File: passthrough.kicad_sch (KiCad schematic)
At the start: 20 parts, among them J10 MiniFit, J13 MiniFit, J5 Pixhawk 1, J6 Pixhawk 2, U17 TLA2528

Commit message: improvements with derick
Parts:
- added D20: RED, LED_SMD:LED_0603_1608Metric, symbol Device:LED
- added D22: 15V, Diode_SMD:D_SOD-523, symbol Device:D_Zener
- added Q3: MMBT5551L, Package_TO_SOT_SMD:SOT-23, symbol Transistor_BJT:MMBT5551L
- added Q4: FDC5614P, Package_TO_SOT_SMD:TSOT-23-6, symbol Transistor_FET:Q_PMOS_DGS
- added R78: 24K, Resistor_SMD:R_0402_1005Metric, symbol Device:R
- added R84: 10K, Resistor_SMD:R_0402_1005Metric, symbol Device:R
- added R85: 1K, Resistor_SMD:R_0402_1005Metric, symbol Device:R
- D15: now not fitted
- R73, R75, TP11: now left out of the parts list
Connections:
- net +BATT: now also D22.2 (A), Q4.1 (D), Q4.2 (D), Q4.5 (D), Q4.6 (D)
- net GND: now also Q3.2 (E), R78.2, R84.1
- new net: D20.1 (K), R78.1
- new net: D20.2 (A), Q4.4 (S)
- new net: D22.1 (K), Q3.3 (C), Q4.3 (G), R84.2
- new net: Q3.1 (B), R85.2
- new net ~{FAULT}: R85.1
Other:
- note added: "FAULT LED INDICATOR - 50V with 3.3V MCU Control LED ON (fault): MCU OFF or GPIO LOW LED OFF (ok): MCU ON with GPIO HIGH (3.3V) PROTECTION: Zener D1 clamps Vgs to -15V (prevents gate overvoltage) R2 pull-down ensures clean gate switchingNPN Q2 inverts logic & isolates 3.3V from 50V railR3 limits base current to safe MCU levels OPERATION: GPIO LOW → Q2 OFF → R2 pulls gate LOW → Vgs = -15V → Q1 ON →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"
- note added: "Fault LED"

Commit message: final export of r1 after changes
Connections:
- net IPAYLOAD renamed IPAYLOAD1
- net RESV0 renamed IPAYLOAD2
- net RESV1 renamed IPAYLOAD3
- net RESV2 renamed VBAT_SCALED
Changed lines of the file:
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@@
 		)
 	)
-	(hierarchical_label "RESV0"
+	(hierarchical_label "IPAYLOAD2"
 		(shape input)
 		(at 217.17 54.61 0)
@@
 		)
 	)
-	(hierarchical_label "RESV1"
+	(hierarchical_label "IPAYLOAD3"
 		(shape input)
 		(at 217.17 57.15 0)
@@
 		)
 	)
-	(hierarchical_label "IPAYLOAD"
+	(hierarchical_label "IPAYLOAD1"
 		(shape input)
 		(at 217.17 52.07 0)
@@
 		)
 	)
-	(hierarchical_label "RESV2"
+	(hierarchical_label "VBAT_SCALED"
 		(shape input)
 		(at 217.17 59.69 0)
@@
 		)
 	)
-	(hierarchical_label "RESV2"
+	(hierarchical_label "VBAT_SCALED"
 		(shape input)
 		(at 198.12 130.81 0)

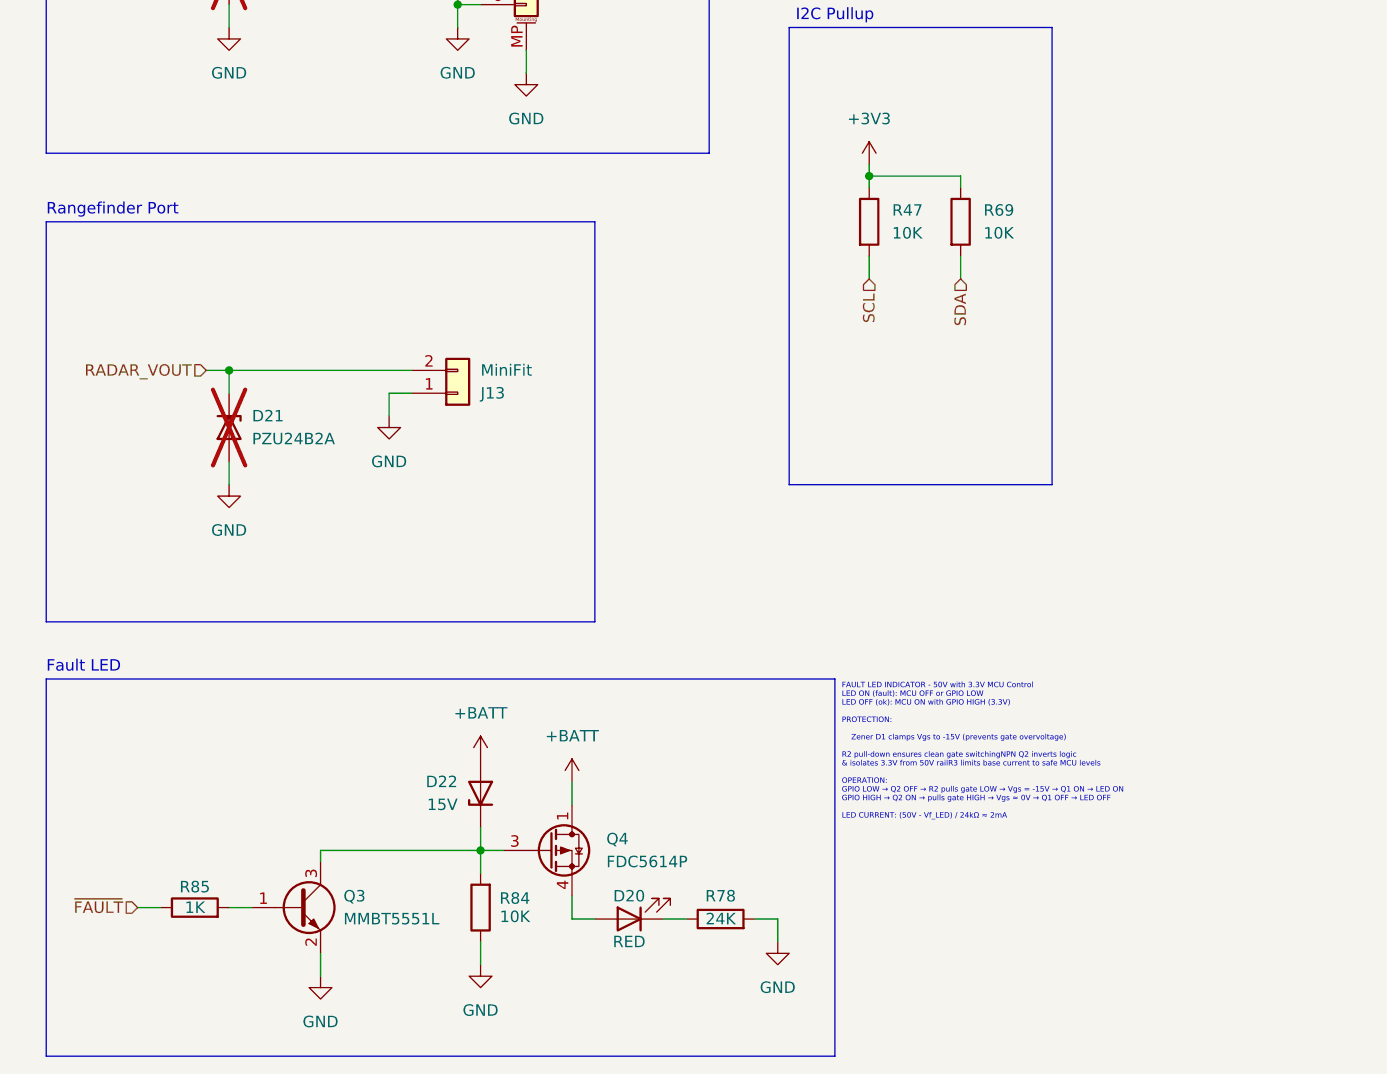
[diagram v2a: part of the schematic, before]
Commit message: created new fault circuitry and assignemd compoennts, need to perform layout
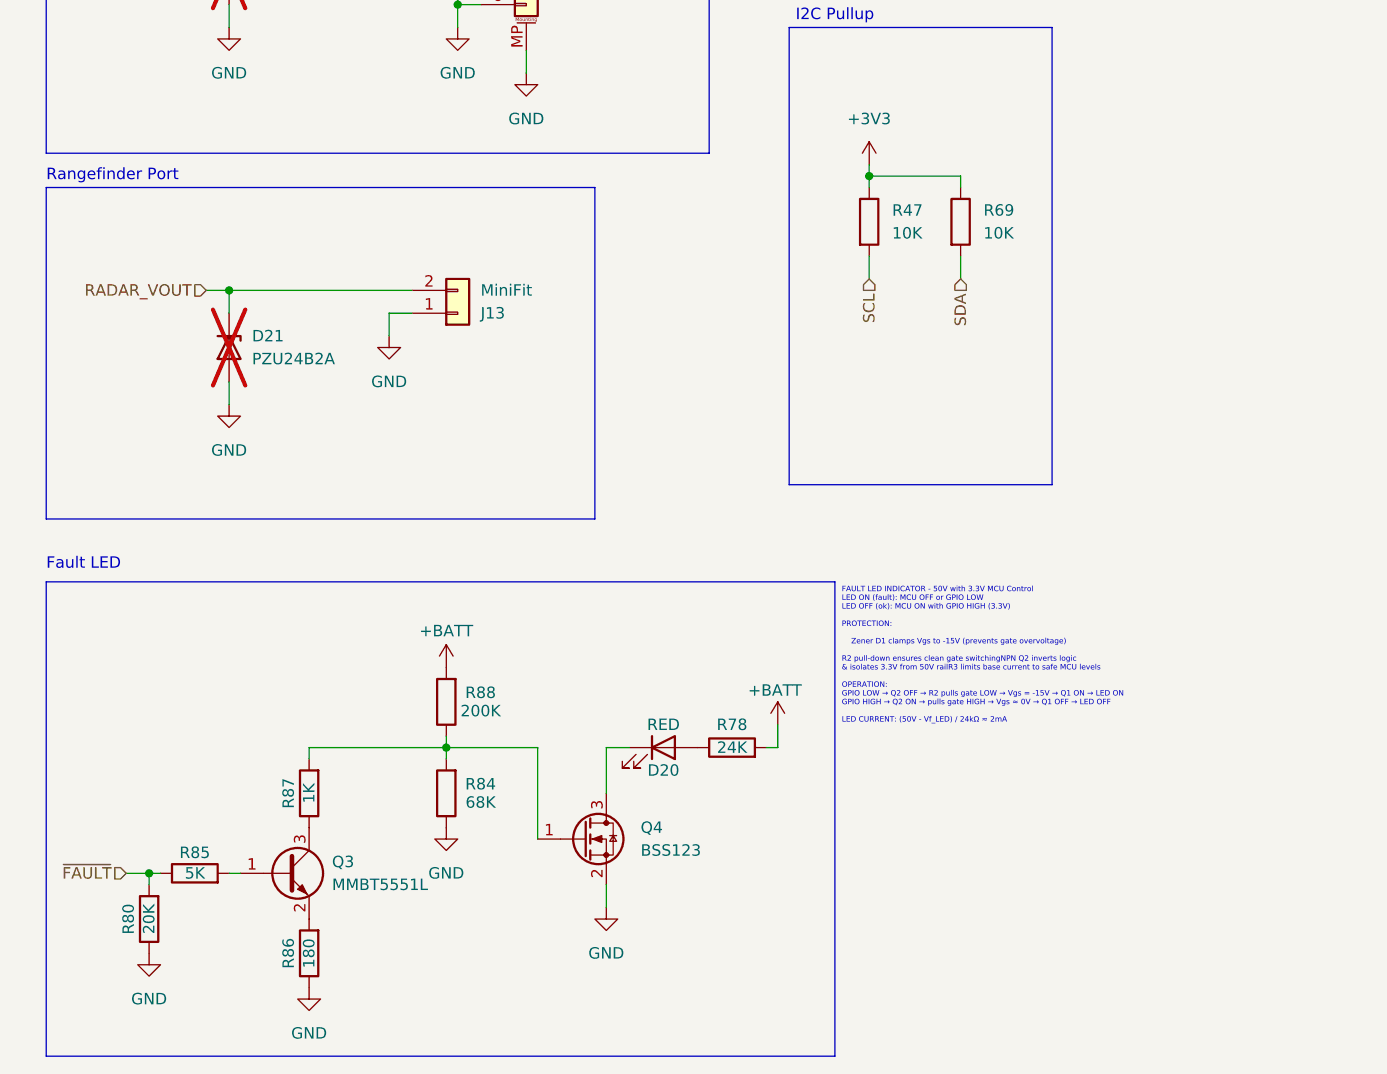
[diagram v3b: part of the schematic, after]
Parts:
- removed D22: 15V, Diode_SMD:D_SOD-523, symbol Device:D_Zener
- removed Q4: FDC5614P, Package_TO_SOT_SMD:TSOT-23-6, symbol Transistor_FET:Q_PMOS_DGS
- added Q4: BSS123, Package_TO_SOT_SMD:SOT-23, symbol Transistor_FET:BSS123
- added R80: 20K, Resistor_SMD:R_0402_1005Metric, symbol Device:R
- added R86: 180, Resistor_SMD:R_0402_1005Metric, symbol Device:R
- added R87: 1K, Resistor_SMD:R_0402_1005Metric, symbol Device:R
- added R88: 200K, Resistor_SMD:R_0402_1005Metric, symbol Device:R
- R84: value 10K -> 68K
- R85: value 1K -> 5K
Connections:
- net +BATT: now also R78.2, R88.2
- net GND: now also Q4.2 (S), R80.1, R86.1; no longer Q3.2 (E), R78.2
- net ~{FAULT}: now also R80.2
- net at D20.1 (K): now also Q4.3 (D); no longer R78.1
- net at D20.2 (A): now also R78.1
- net at R84.2: now also Q4.1 (G), R87.2, R88.1; no longer Q3.3 (C)
- new net: Q3.2 (E), R86.2
- new net: Q3.3 (C), R87.1
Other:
- moved on the sheet: D20, D21, J13, Q3, R78, R84, R85

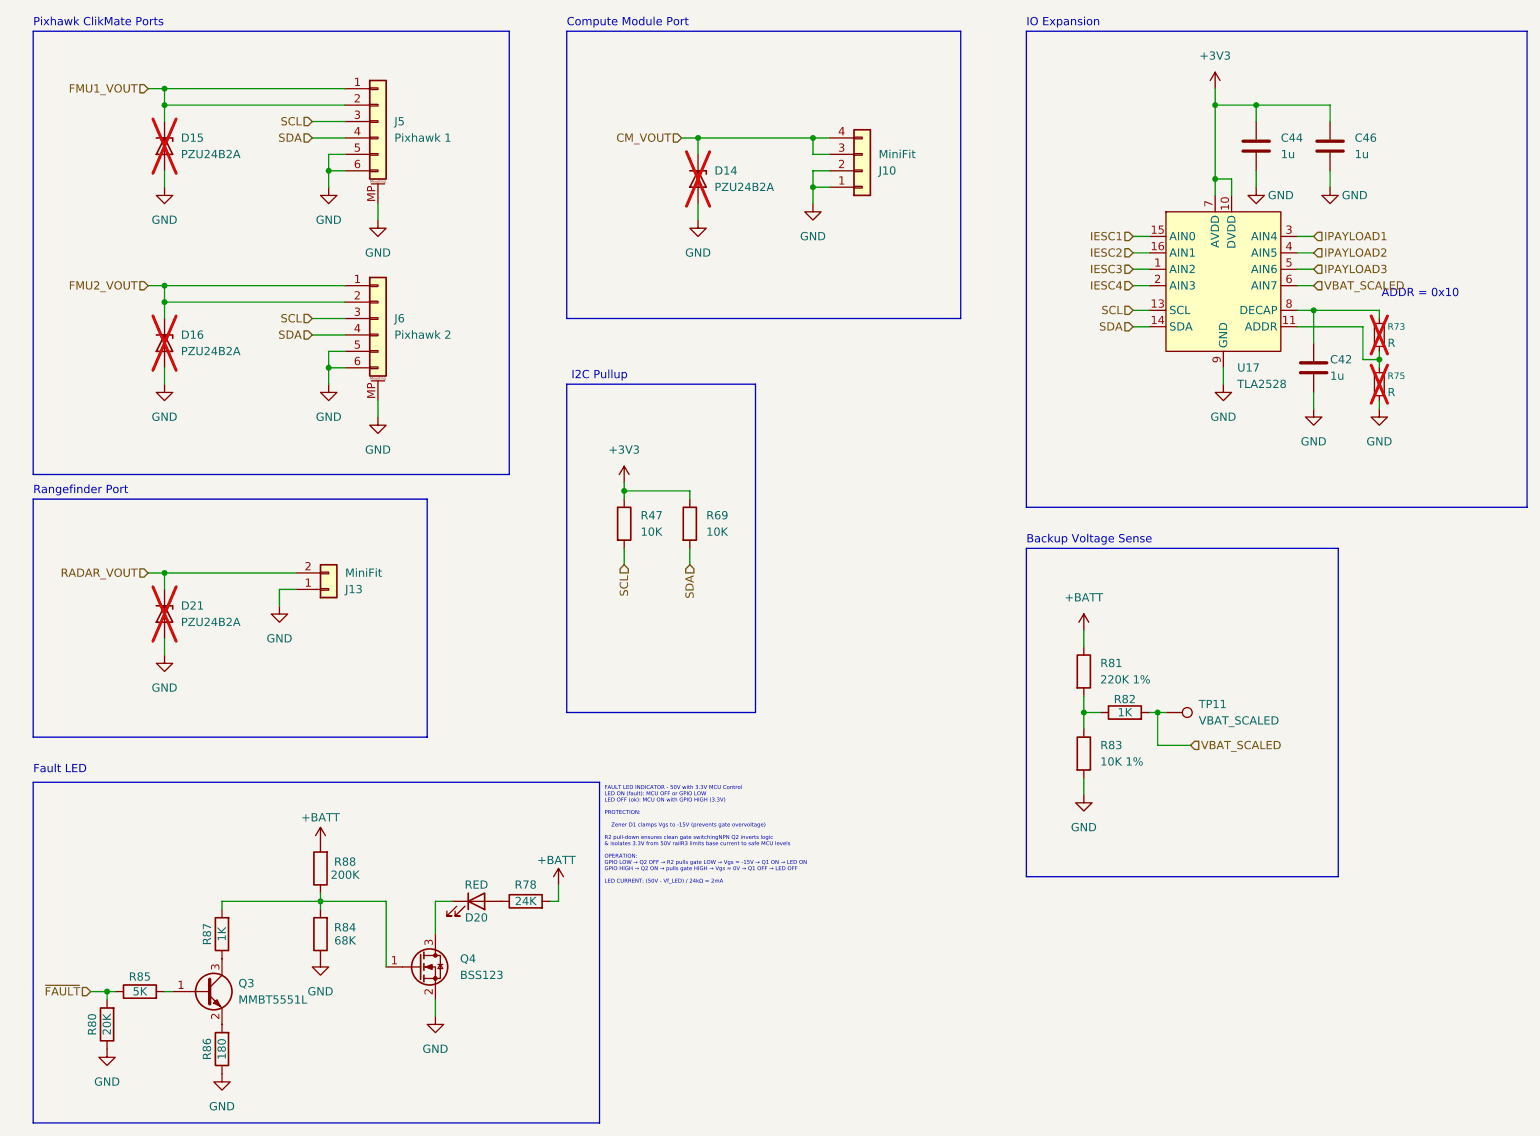
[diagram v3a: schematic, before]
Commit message: updated layout for fault led with new circuit, rerouted
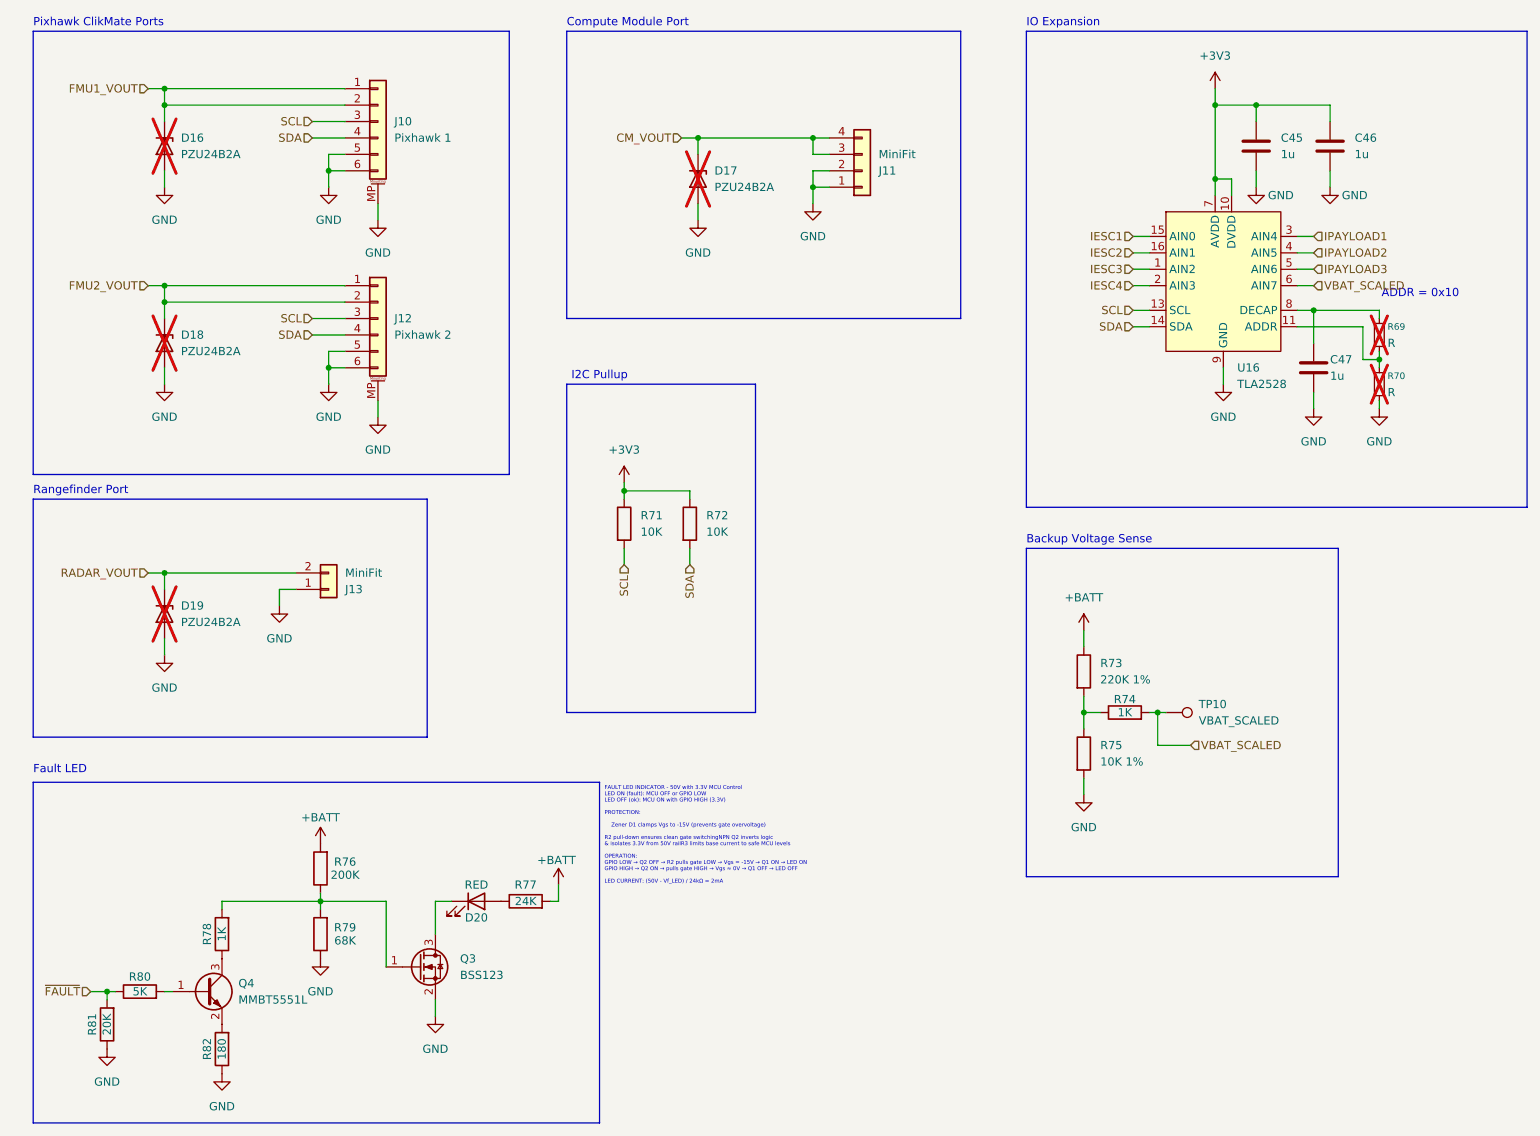
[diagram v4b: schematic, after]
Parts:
- renumbered C44 to C45, C42 to C47, D15 to D16, D14 to D17, D16 to D18, D21 to D19, J5 to J10, J10 to J11, J6 to J12, Q4 to Q3, Q3 to Q4, R73 to R69, R75 to R70, R47 to R71, R69 to R72, R81 to R73, R82 to R74, R83 to R75, R88 to R76, R78 to R77, R87 to R78, R84 to R79, R85 to R80, R80 to R81, R86 to R82, TP11 to TP10, U17 to U16
